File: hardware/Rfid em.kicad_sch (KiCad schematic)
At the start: 18 parts, among them IC1 EM4095, J1 Conn_01x06, U1 560uH, U2 AMS1117-5.0

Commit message: fix: Add 10µF input capacitor for AMS1117-5.0
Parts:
- added C8: 10 uF, Capacitor_SMD:C_0805_2012Metric, symbol Device:C_Small_US
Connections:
- net GND: now also C8.2
- net at J1.1 (Pin_1), U2.3 (VI): now also C8.1

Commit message: fix: Specify capacitor parts and place decoupling caps per datasheets
Use tantalum capacitors with MPNs for the AMS1117-5.0 (10µF input, 22µF output) and add a 100nF decoupling capacitor for the EM4095. Place C8 at U2 VIN, C1 at the U2 VOUT tab and C9 across IC1 DVDD/DVSS, link the footprints to their schematic symbols and move C9 into the schematic frame.
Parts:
- added C9: 100 nF, Capacitor_SMD:C_0805_2012Metric, symbol Device:C_Small_US
- C1: value 100 nF -> 22 uF; footprint Capacitor_SMD:C_0805_2012Metric -> Capacitor_Tantalum_SMD:CP_EIA-3528-21_Kemet-B; symbol Device:C_Small_US -> Device:C_Polarized_Small_US; MPN (none) -> T491B226K016AT; Manufacturer (none) -> KEMET
- C8: footprint Capacitor_SMD:C_0805_2012Metric -> Capacitor_Tantalum_SMD:CP_EIA-3216-18_Kemet-A; symbol Device:C_Small_US -> Device:C_Polarized_Small_US; MPN (none) -> T491A106K016AT; Manufacturer (none) -> KEMET
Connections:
- net GND: now also C9.1
- net VDD: now also C9.2

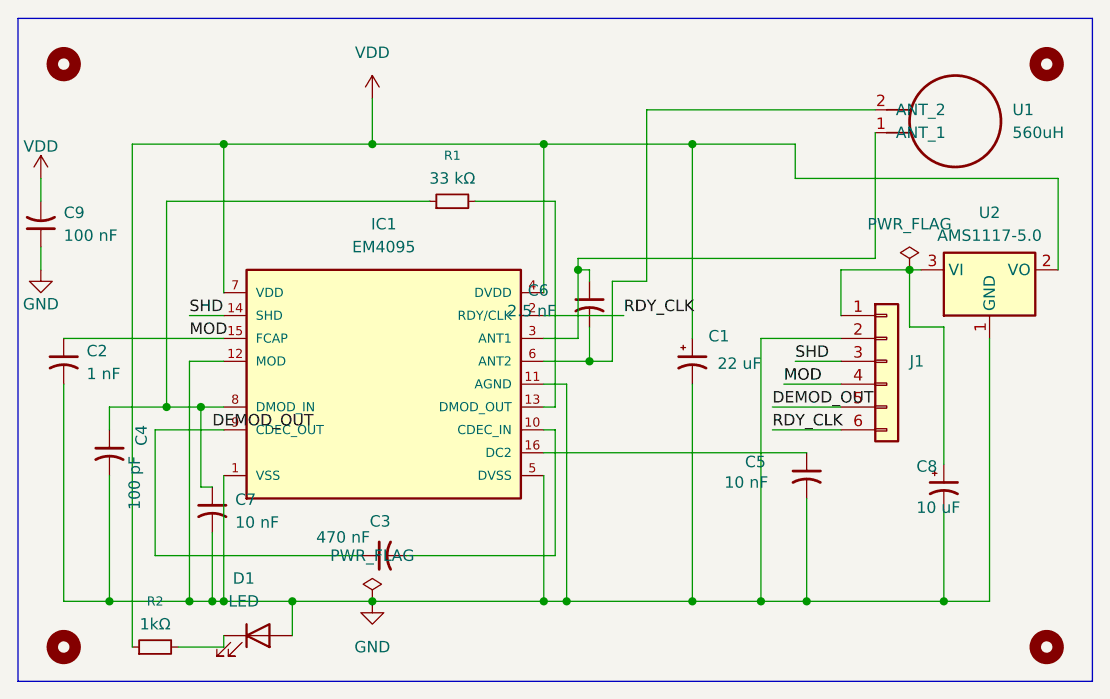
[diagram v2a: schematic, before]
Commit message: fix: Add MPNs, generate BOM from schematic and improve decoupling
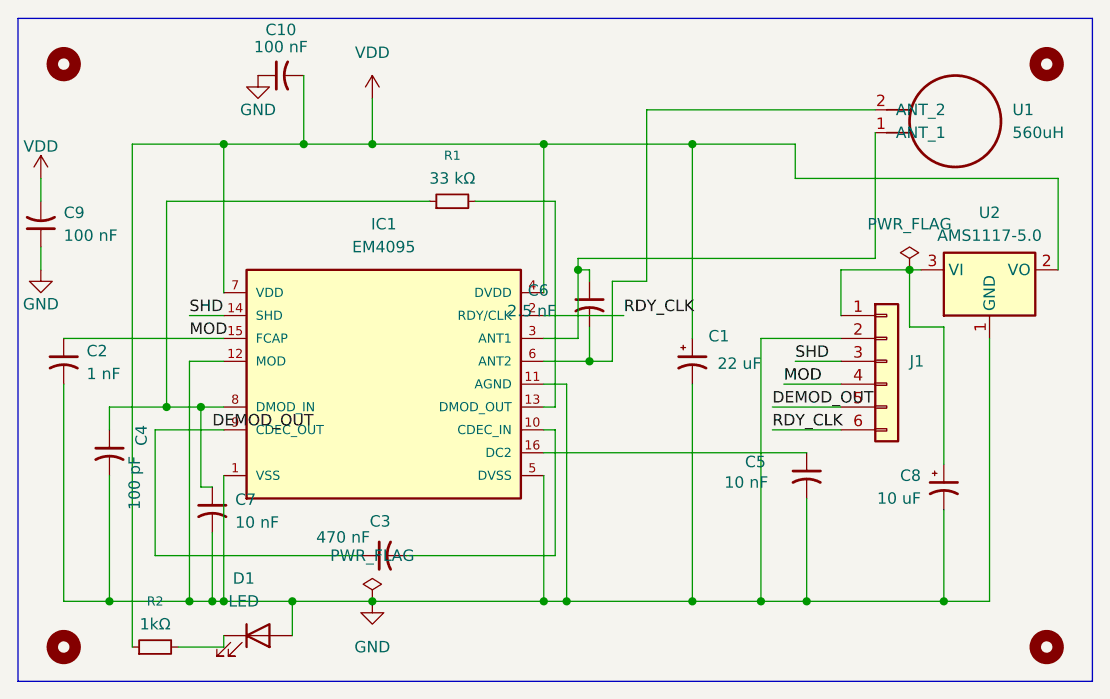
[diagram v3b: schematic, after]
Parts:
- added C10: 100 nF, Capacitor_SMD:C_0603_1608Metric, symbol Device:C_Small_US
- C1: Name (none) -> Tantalum Capacitor
- C2: Buying Links (none) -> 1nF 102 0805 (2012 metric) 50V X7R MLCC SMD [4035] : Sunrom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; Name (none) -> SMD Capacitor
- C3: Buying Links (none) -> 470nF 474 0805 (2012 metric) 50V X7R MLCC SMD [3944] : Sunr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; Name (none) -> SMD Capacitor
- C4: Buying Links (none) -> 100pF 101 0805 (2012 metric) 50V X7R MLCC SMD [4479] : Sunr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; Name (none) -> SMD Capacitor
- C5, C7: Buying Links (none) -> 10nF 103 0805 (2012 metric) 50V X7R MLCC SMD [4034] : Sunro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; Name (none) -> SMD Capacitor
- C6: Buying Links (none) -> 08055C242KAT2A KYOCERA AVX | Mouser India; Name (none) -> SMD Capacitor
- C8: footprint Capacitor_Tantalum_SMD:CP_EIA-3216-18_Kemet-A -> Capacitor_Tantalum_SMD:CP_EIA-6032-28_Kemet-C; MPN T491A106K016AT -> T491C106K035AT; Name (none) -> Tantalum Capacitor
- C9: Name (none) -> SMD Capacitor
- D1: Buying Links (none) -> Buy 1206 Surface mount LED White Online at Best Price | Rob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; Name (none) -> SMD LED
- IC1: Buying Links (none) -> EM4095HMSO16B+ EM Microelectronic | RF and Wireless | DigiK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; Name (none) -> IC
- J1: Buying Links (none) -> Buy Header Pins 40x1 - 2.54mm Pitch - Brass - KTRON India; Name (none) -> 6 Pin Connector
- R1: Buying Links (none) -> 33K 1% 0805 [4321] : Sunrom Electronics; Name (none) -> SMD Resistor
- R2: Buying Links (none) -> Buy RT1206FRE071KL Resistors Online in India | Robu.in; Name (none) -> SMD Resistor
- U1: now left out of the parts list
- U2: Buying Links (none) -> https://www.sunrom.com/p/1117-5v-1a-sot223-low-drop-linear-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; MPN (none) -> AMS1117-5.0; Manufacturer (none) -> Advanced Monolithic Systems; Name (none) -> Voltage Regulator
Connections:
- net GND: now also C10.1
- net VDD: now also C10.2
